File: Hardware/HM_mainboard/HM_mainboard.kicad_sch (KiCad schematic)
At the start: 0 parts

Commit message: Updated BOM
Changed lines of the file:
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@@
     (stroke (width 0) (type default))
   )
-  (wire (pts (xy 45.72 52.07) (xy 50.165 52.07))
+  (wire (pts (xy 46.355 52.07) (xy 50.165 52.07))
     (stroke (width 0) (type default))
   )
@@
   )
   (label "LED_DEV_R" (at 45.72 69.215 180) (fields_autoplaced)
+    (effects (font (size 1.27 1.27)) (justify right bottom))
+  )
+  (label "BATT_CHARGING_STATUS" (at 46.355 52.07 180) (fields_autoplaced)
     (effects (font (size 1.27 1.27)) (justify right bottom))
   )
@@
     (effects (font (size 1.27 1.27)) (justify right bottom))
   )
-  (label "BATT_CHARGING_STATUS" (at 45.72 52.07 180) (fields_autoplaced)
-    (effects (font (size 1.27 1.27)) (justify right bottom))
-  )

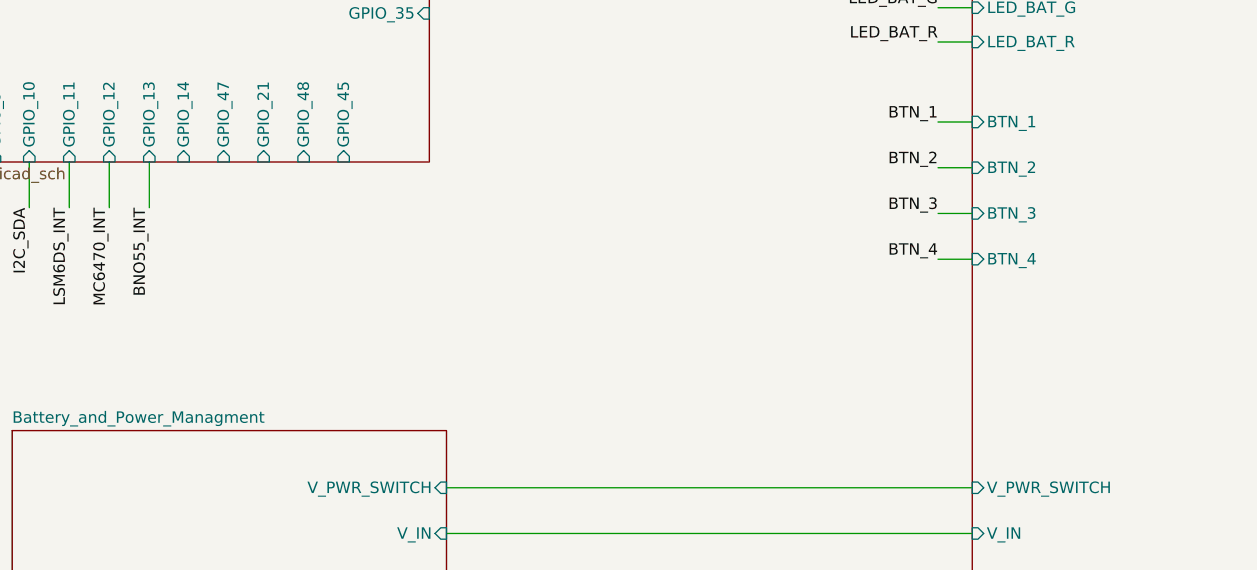
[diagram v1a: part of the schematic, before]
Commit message: Added connector for sip&puff sensor
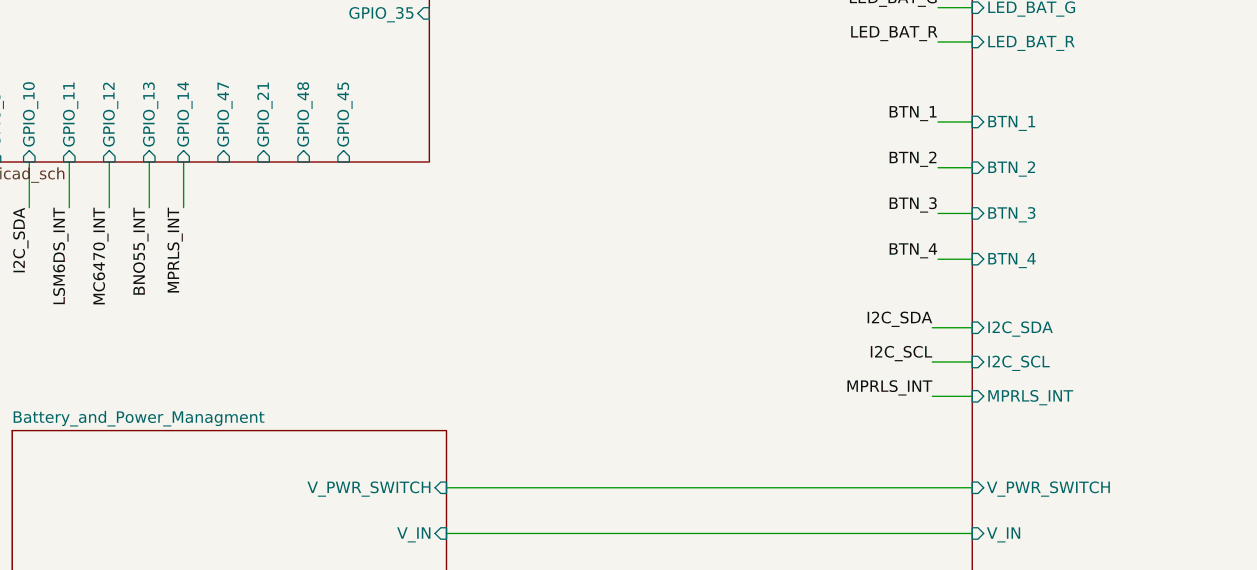
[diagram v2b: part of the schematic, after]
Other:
- sheet UI_Peripherals ports: added I2C_SCL, I2C_SDA, MPRLS_INT; removed none
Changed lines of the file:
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@@
+    (stroke (width 0) (type default))
+  )
+  (wire (pts (xy 172.72 129.54) (xy 177.165 129.54))
     (stroke (width 0) (type default))
   )
@@
     (stroke (width 0) (type default))
   )
+  (wire (pts (xy 172.72 125.73) (xy 177.165 125.73))
+    (stroke (width 0) (type default))
+  )
   (wire (pts (xy 173.355 90.17) (xy 177.165 90.17))
     (stroke (width 0) (type default))
@@
     (stroke (width 0) (type default))
   )
+  (wire (pts (xy 172.72 121.92) (xy 177.165 121.92))
+    (stroke (width 0) (type default))
+  )
   (wire (pts (xy 173.355 114.3) (xy 177.165 114.3))
     (stroke (width 0) (type default))
@@
     (stroke (width 0) (type default))
   )
+  (wire (pts (xy 89.535 103.505) (xy 89.535 108.585))
+    (stroke (width 0) (type default))
+  )
   (wire (pts (xy 45.72 55.88) (xy 50.165 55.88))
     (stroke (width 0) (type default))
@@
     (effects (font (size 1.27 1.27)) (justify left bottom))
   )
+  (label "I2C_SDA" (at 172.72 121.92 180) (fields_autoplaced)
+    (effects (font (size 1.27 1.27)) (justify right bottom))
+  )
   (label "BTN_1" (at 173.355 99.06 180) (fields_autoplaced)
     (effects (font (size 1.27 1.27)) (justify right bottom))
@@
     (effects (font (size 1.27 1.27)) (justify right bottom))
   )
+  (label "I2C_SCL" (at 172.72 125.73 180) (fields_autoplaced)
+    (effects (font (size 1.27 1.27)) (justify right bottom))
+  )
   (label "LSM6DS_INT" (at 175.26 42.545 180) (fields_autoplaced)
     (effects (font (size 1.27 1.27)) (justify right bottom))
@@
     (effects (font (size 1.27 1.27)) (justify right bottom))
   )
+  (label "MPRLS_INT" (at 89.535 108.585 270) (fields_autoplaced)
+    (effects (font (size 1.27 1.27)) (justify right bottom))
+  )
   (label "LSM6DS_INT" (at 76.835 108.585 270) (fields_autoplaced)
     (effects (font (size 1.27 1.27)) (justify right bottom))
@@
   )
   (label "LED_DEV_G" (at 45.72 73.025 180) (fields_autoplaced)
+    (effects (font (size 1.27 1.27)) (justify right bottom))
+  )
+  (label "MPRLS_INT" (at 172.72 129.54 180) (fields_autoplaced)
     (effects (font (size 1.27 1.27)) (justify right bottom))
   )
@@
       (effects (font (size 1.27 1.27)) (justify left))
     )
+    (pin "I2C_SDA" input (at 177.165 121.92 180)
+      (effects (font (size 1.27 1.27)) (justify left))
+    )
+    (pin "I2C_SCL" input (at 177.165 125.73 180)
+      (effects (font (size 1.27 1.27)) (justify left))
+    )
+    (pin "MPRLS_INT" input (at 177.165 129.54 180)
+      (effects (font (size 1.27 1.27)) (justify left))
+    )

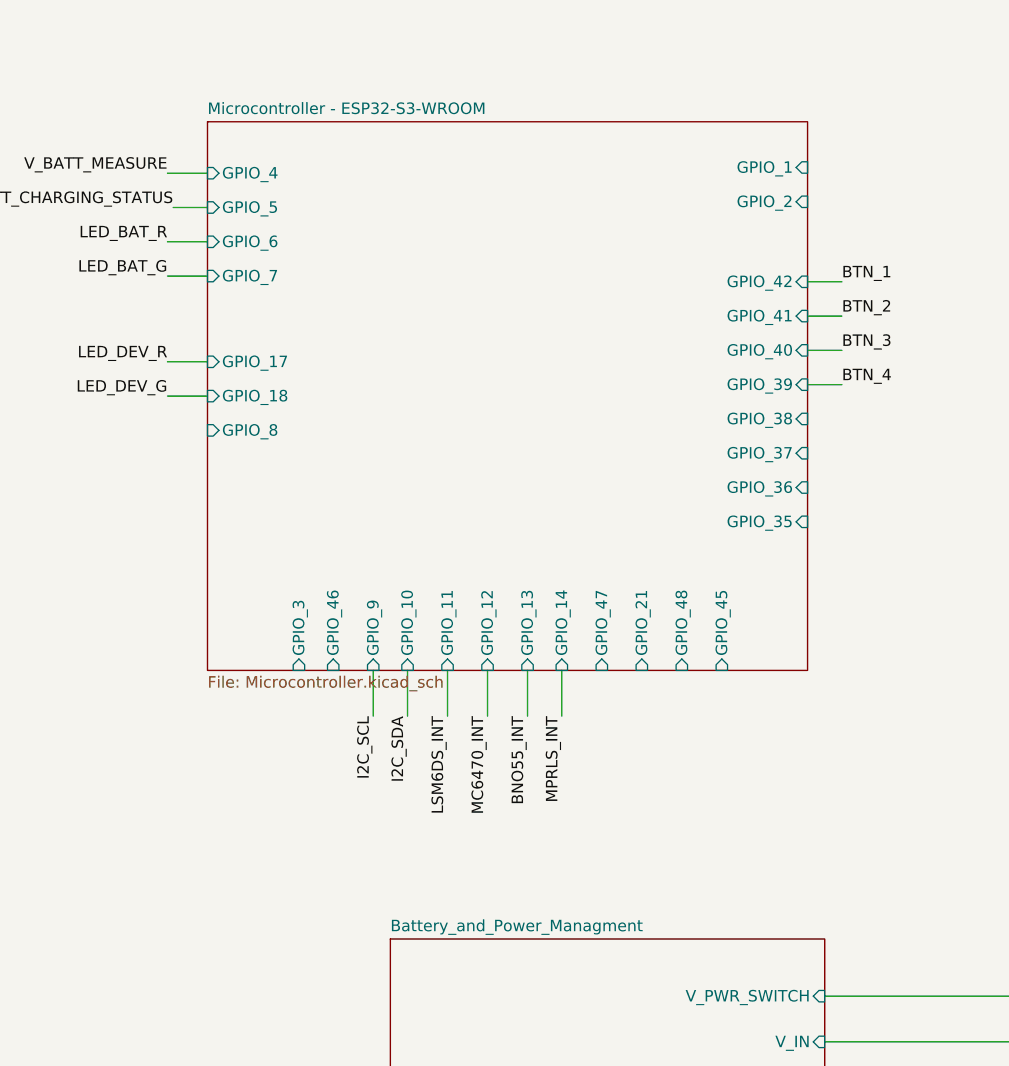
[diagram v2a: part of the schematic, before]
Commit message: Updated schematic and PCB according to Email from BA on 16th of April
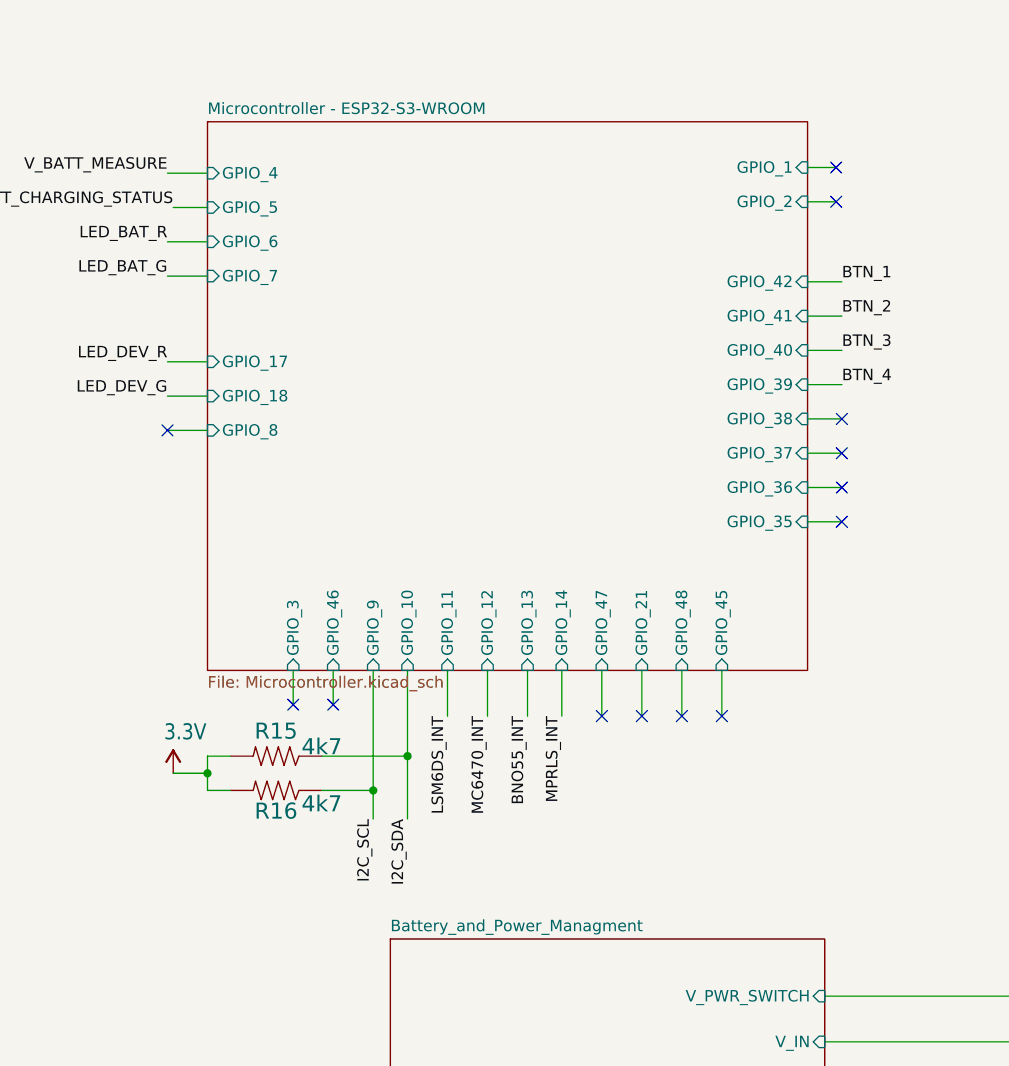
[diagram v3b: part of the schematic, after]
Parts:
- added R15, R16: 4k7, Resistor_SMD:R_0603_1608Metric_Pad0.98x0.95mm_HandSolder, symbol esp32-thing-eagle-import:10KOHM-1/10W-1%(0603)0603
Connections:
- net I2C_SCL: now also R16.1
- net I2C_SDA: now also R15.1
- new net 3.3V: R15.2, R16.2
- no-connect marks 0 -> 13

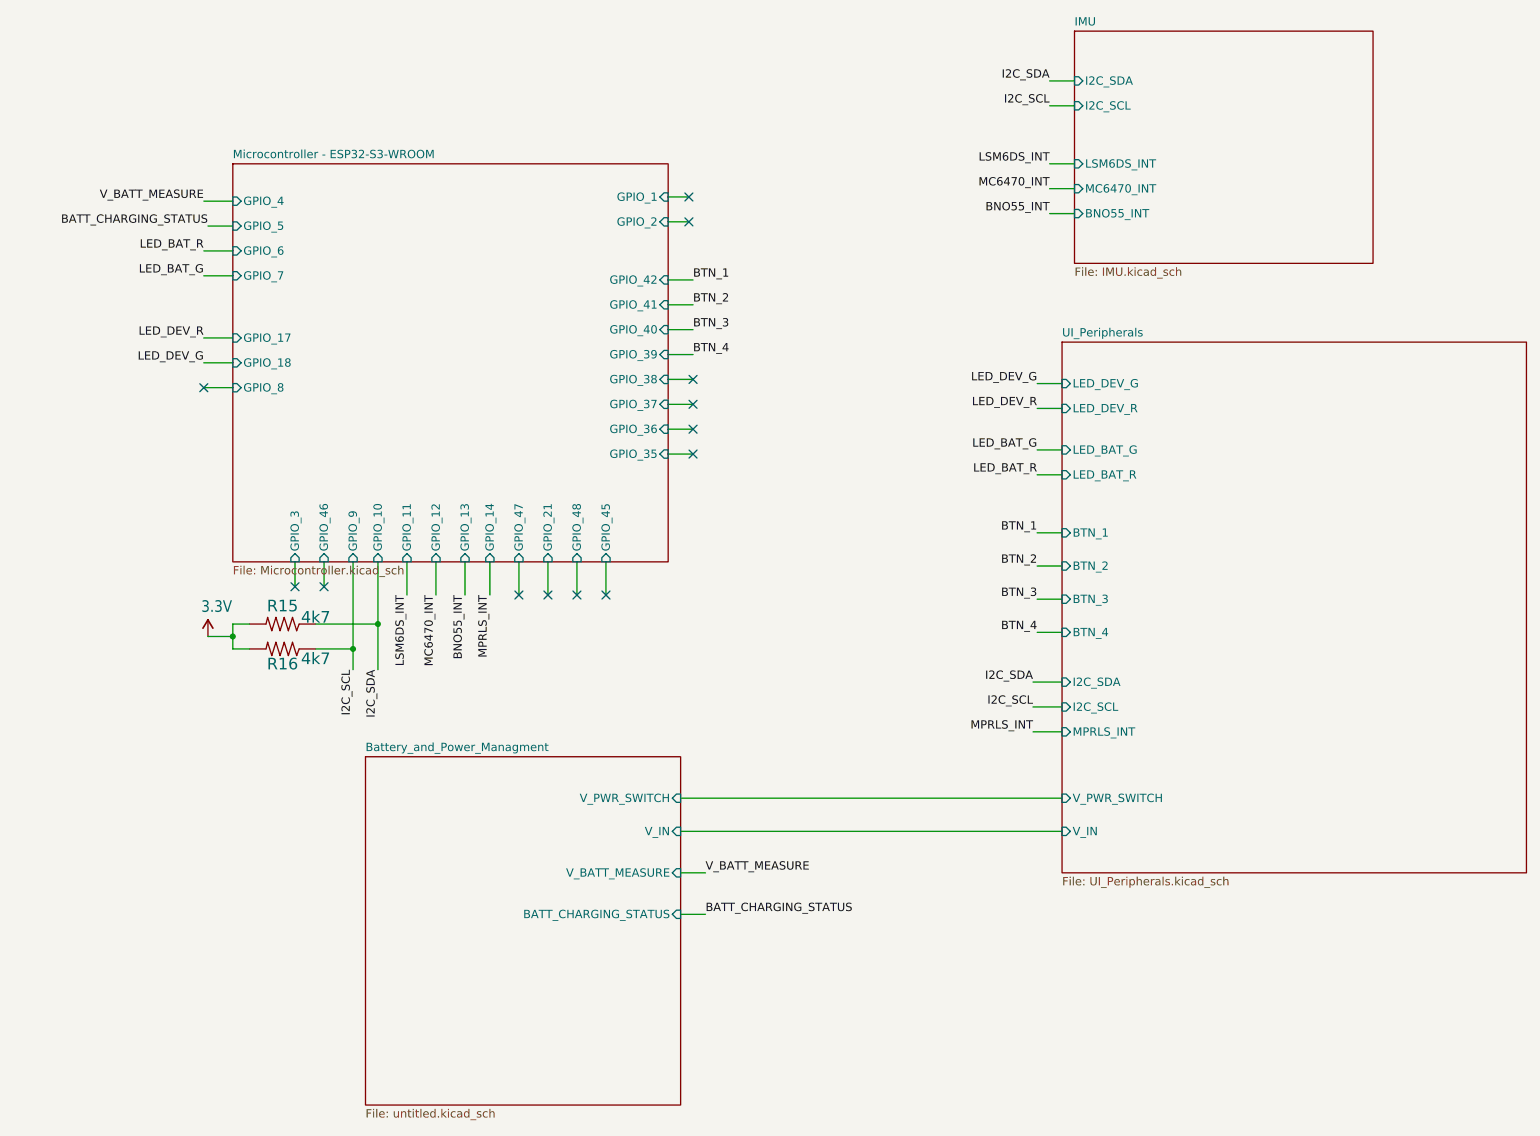
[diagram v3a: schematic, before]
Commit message: Updated schematic to version v2.0.0
•	Removed two 6-Axis IMUs
•	As the BNO055 did not respond to I2C requests, a 2k7 pullup was added in parallel to the I2C-SDA pullup. The behavior is described here:  https://forums.adafruit.com/viewtopic.php?t=205215
•	Added mounting holes for enclosure
•	Added board description prints
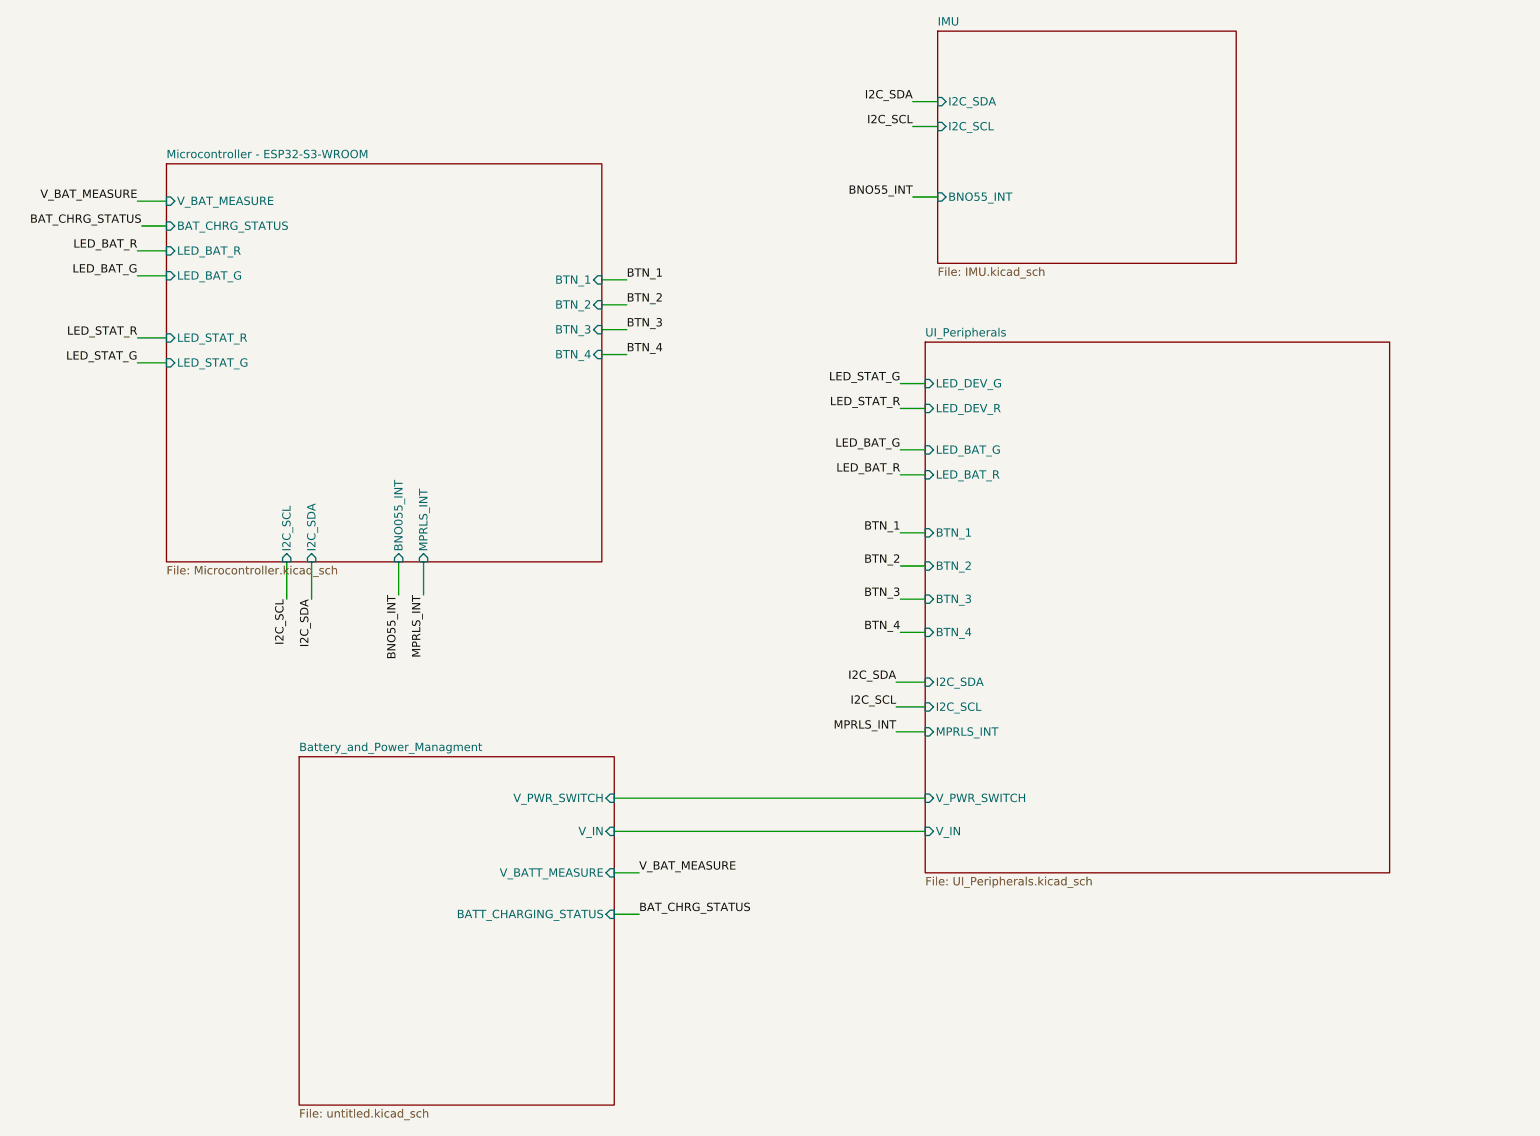
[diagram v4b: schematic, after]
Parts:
- removed R15, R16: 4k7, Resistor_SMD:R_0603_1608Metric_Pad0.98x0.95mm_HandSolder, symbol esp32-thing-eagle-import:10KOHM-1/10W-1%(0603)0603
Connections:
- no-connect marks 13 -> 0
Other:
- sheet IMU ports: added none; removed LSM6DS_INT, MC6470_INT
- sheet Microcontroller - ESP32-S3-WROOM ports: added BAT_CHRG_STATUS, BNO055_INT, BTN_1, BTN_2, BTN_3, BTN_4, I2C_SCL, I2C_SDA, LED_BAT_G, LED_BAT_R, LED_STAT_G, LED_STAT_R, MPRLS_INT, V_BAT_MEASURE; removed GPIO_1, GPIO_10, GPIO_11, GPIO_12, GPIO_13, GPIO_14, GPIO_17, GPIO_18, GPIO_2, GPIO_21, GPIO_3, GPIO_35, GPIO_36, GPIO_37, GPIO_38, GPIO_39, GPIO_4, GPIO_40, GPIO_41, GPIO_42, GPIO_45, GPIO_46, GPIO_47, GPIO_48, GPIO_5, GPIO_6, GPIO_7, GPIO_8, GPIO_9
